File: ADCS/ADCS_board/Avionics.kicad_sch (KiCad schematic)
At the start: 45 parts, among them SW1 KMR231NG LFS, SW2 KMR231NG LFS, U14 LTC2309xF, U2 RP2350_80QFN, U3 MR25H40MDF, Y1 ABM8-272-T3

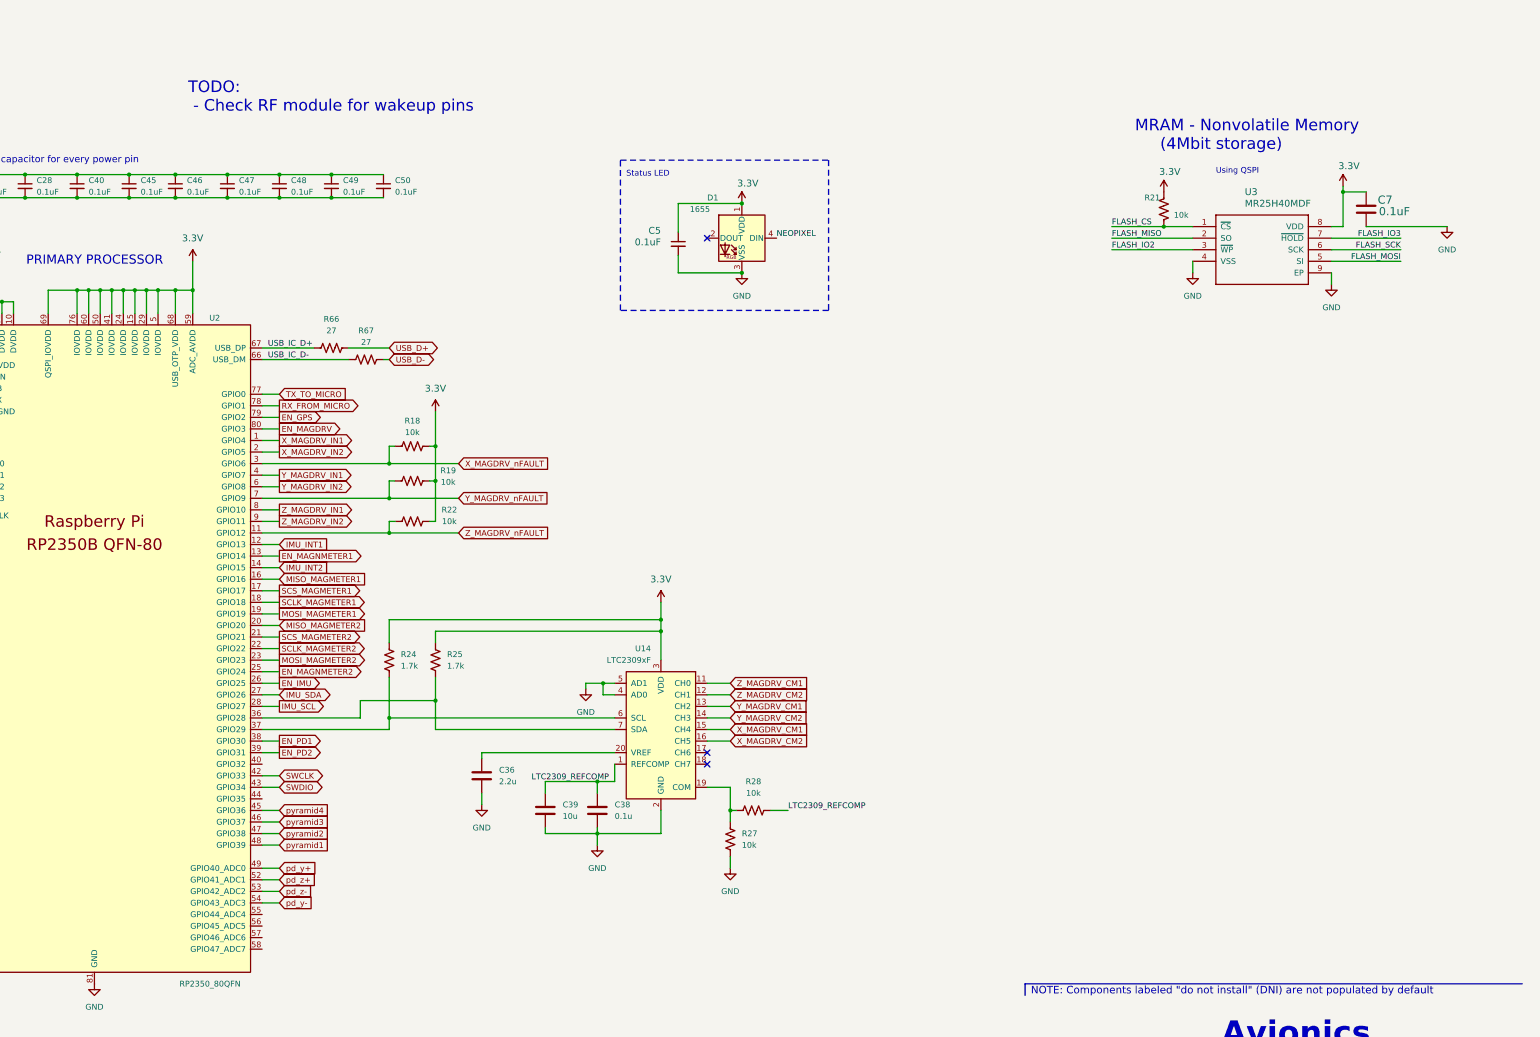
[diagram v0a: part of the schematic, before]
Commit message: main adcs board with initial traces coming out of MCU
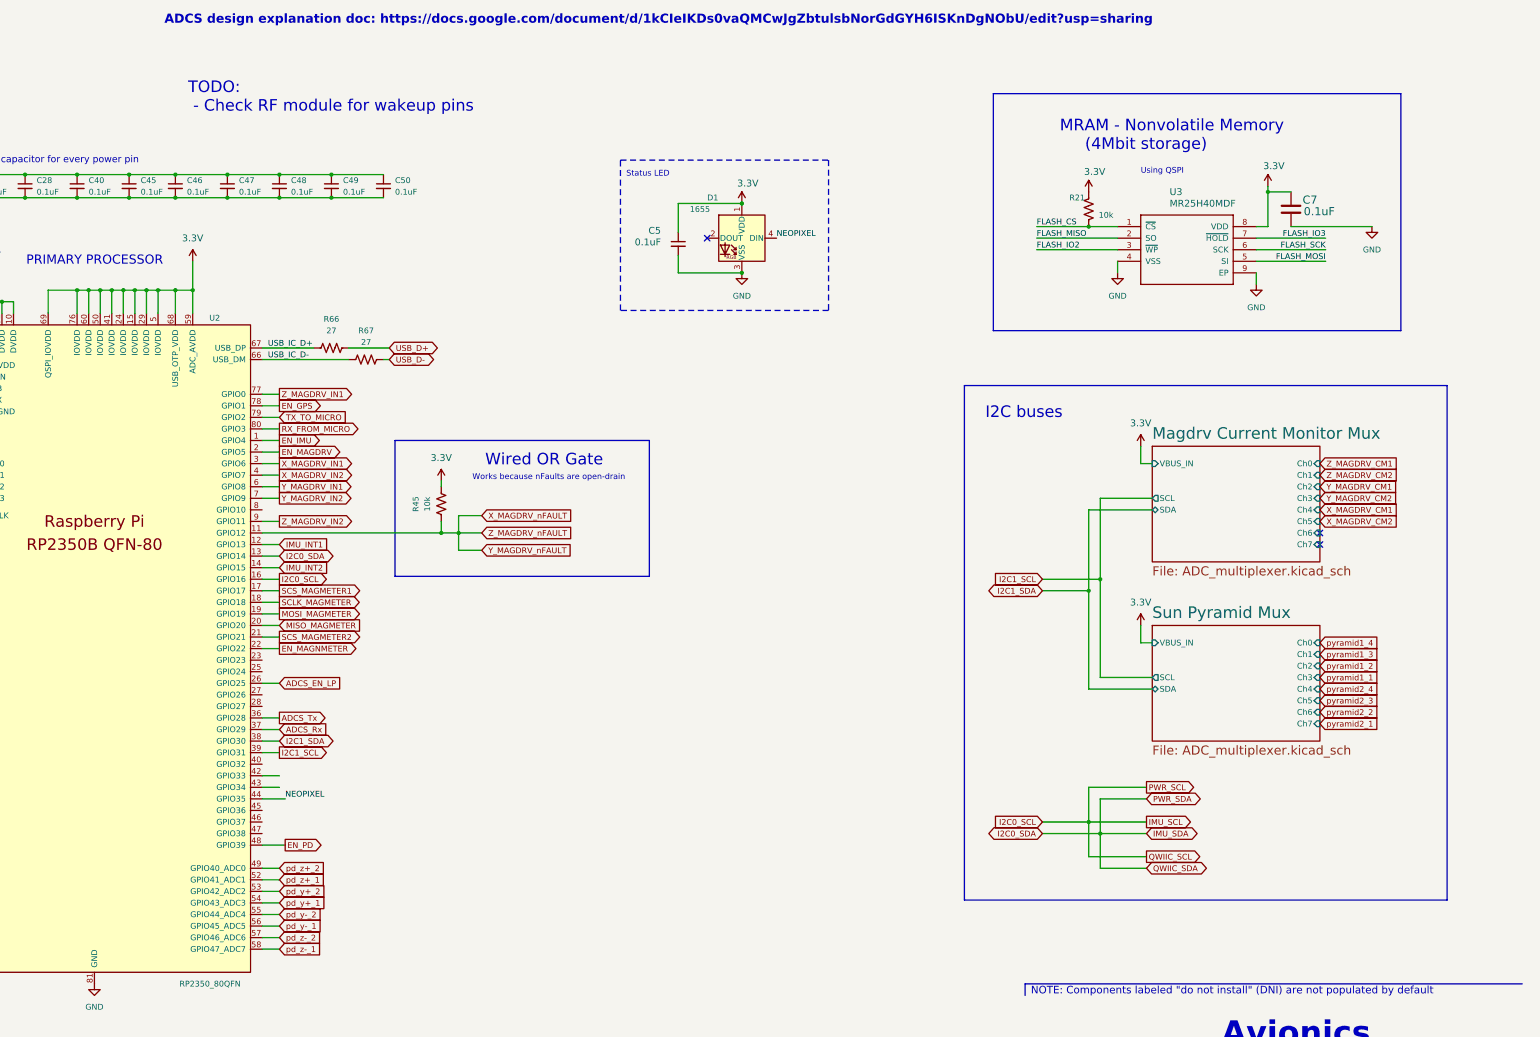
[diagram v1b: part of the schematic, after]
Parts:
- removed C36: 2.2u, Capacitor_SMD:C_0603_1608Metric, symbol Device:C
- removed C38: 0.1u, Capacitor_SMD:C_0603_1608Metric, symbol Device:C
- removed C39: 10u, Capacitor_SMD:C_0603_1608Metric, symbol Device:C
- removed R18, R19, R22, R27, R28: 10k, Resistor_SMD:R_0603_1608Metric, symbol Device:R_US
- removed R24, R25: 1.7k, Resistor_SMD:R_0603_1608Metric, symbol Device:R_US
- removed U14: LTC2309xF, Package_SO:TSSOP-20_4.4x6.5mm_P0.65mm, symbol Analog_ADC:LTC2309xF
- added R45: 10k, Resistor_SMD:R_0603_1608Metric, symbol Device:R_US
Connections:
- net Y_MAGDRV_nFAULT is gone; now on net Y_MAGDRV_IN2: U2.7 (GPIO9)
- net Z_MAGDRV_nFAULT is gone; now on net X_MAGDRV_nFAULT: U2.11 (GPIO12)
- net 3.3V: now also R45.2
- net EN_GPS: now also U2.78 (GPIO1); no longer U2.79 (GPIO2)
- net EN_IMU: now also U2.1 (GPIO4); no longer U2.26 (GPIO25)
- net EN_MAGDRV: now also U2.2 (GPIO5); no longer U2.80 (GPIO3)
- net NEOPIXEL: now also U2.44 (GPIO35)
- net RX_FROM_MICRO: now also U2.80 (GPIO3); no longer U2.78 (GPIO1)
- net SWCLK: no longer U2.42 (GPIO33)
- net SWDIO: no longer U2.43 (GPIO34)
- net TX_TO_MICRO: now also U2.79 (GPIO2); no longer U2.77 (GPIO0)
- net X_MAGDRV_IN1: now also U2.3 (GPIO6); no longer U2.1 (GPIO4)
- net X_MAGDRV_IN2: now also U2.4 (GPIO7); no longer U2.2 (GPIO5)
- net X_MAGDRV_nFAULT: now also R45.1; no longer U2.3 (GPIO6)
- net Y_MAGDRV_IN1: now also U2.6 (GPIO8); no longer U2.4 (GPIO7)
- net Y_MAGDRV_IN2: no longer U2.6 (GPIO8)
- net Z_MAGDRV_IN1: now also U2.77 (GPIO0); no longer U2.8 (GPIO10)
- net ADCS_Tx: now reaches U2.36 (GPIO28)
- net ADCS_Rx: now reaches U2.37 (GPIO29)
- net pd_y-_2: now reaches U2.55 (GPIO44_ADC4)
- net pd_y-_1: now reaches U2.56 (GPIO45_ADC5)
- net pd_z-_2: now reaches U2.57 (GPIO46_ADC6)
- net pd_z-_1: now reaches U2.58 (GPIO47_ADC7)
- net EN_MAGNMETER1 renamed I2C0_SDA
- net EN_MAGNMETER2: no longer names the net of U2.25 (GPIO24)
- net EN_PD1 renamed I2C1_SDA
- net EN_PD2 renamed I2C1_SCL
- net IMU_SCL: no longer names the net of U2.28 (GPIO27)
- net IMU_SDA: no longer names the net of U2.27 (GPIO26)
- net MISO_MAGMETER1 renamed I2C0_SCL
- net MISO_MAGMETER2 renamed MISO_MAGMETER
- net MOSI_MAGMETER1 renamed MOSI_MAGMETER
- net MOSI_MAGMETER2: no longer names the net of U2.23 (GPIO23)
- net SCLK_MAGMETER1 renamed SCLK_MAGMETER
- net SCLK_MAGMETER2 renamed EN_MAGNMETER
- net pd_y+ renamed pd_z+_2
- net pd_y- renamed pd_y+_1
- net pd_z+ renamed pd_z+_1
- net pd_z- renamed pd_y+_2
- net pyramid1 renamed EN_PD
- net pyramid2: no longer names the net of U2.47 (GPIO38)
- net pyramid3: no longer names the net of U2.46 (GPIO37)
- net pyramid4: no longer names the net of U2.45 (GPIO36)
- new net ADCS_EN_LP: U2.26 (GPIO25)
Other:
- added sheet Magdrv Current Monitor Mux (ADC_multiplexer.kicad_sch)
- added sheet Sun Pyramid Mux (ADC_multiplexer.kicad_sch)
- note added: "ADCS design explanation doc: https://docs.google.com/document/d/1kCIeIKDs0vaQMCwJgZbtulsbNorGdGYH6ISKnDgNObU/edit?usp=sharing"
- note added: "I2C buses"
- note added: "Wired OR Gate"
- note added: "Works because nFaults are open-drain"
- title: PyCubed Mainboard -> ADCS Main Board
- moved on the sheet: C7, R21, U3
